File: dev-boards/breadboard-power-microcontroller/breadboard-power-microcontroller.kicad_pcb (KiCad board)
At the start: 2 copper layers, 51.3 x 22 mm, 28 parts, among them J0 USB_C_Receptacle_PowerOnly_6P, J1 Barrel_Jack_Switch, J2 Conn_01x02, Q1 AO3401A, Q2 AO3401A, SW1 SW_DPDT_x2, U1 AMS1117-5.0, U2 AMS1117-3.3

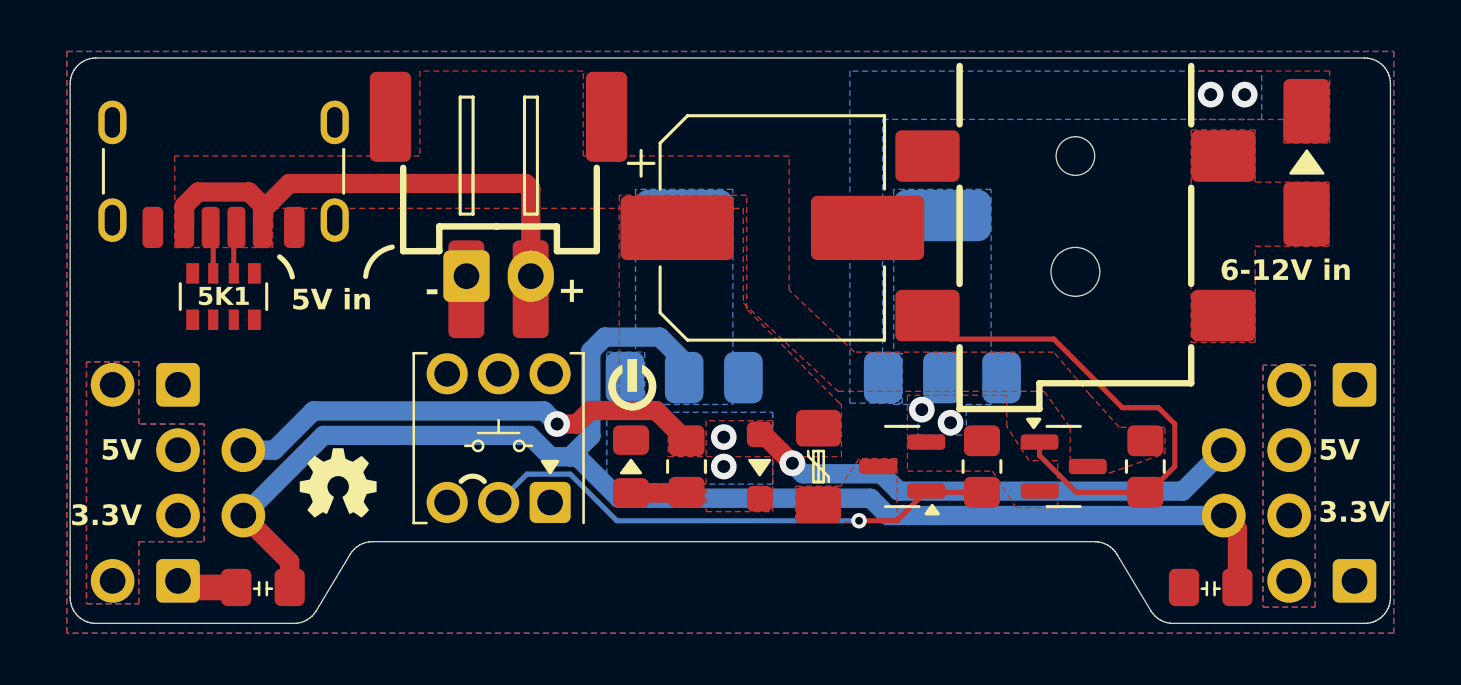
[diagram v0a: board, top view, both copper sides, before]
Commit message: Replace AMS1117 with MT6211 on breadboard microcontroller power board
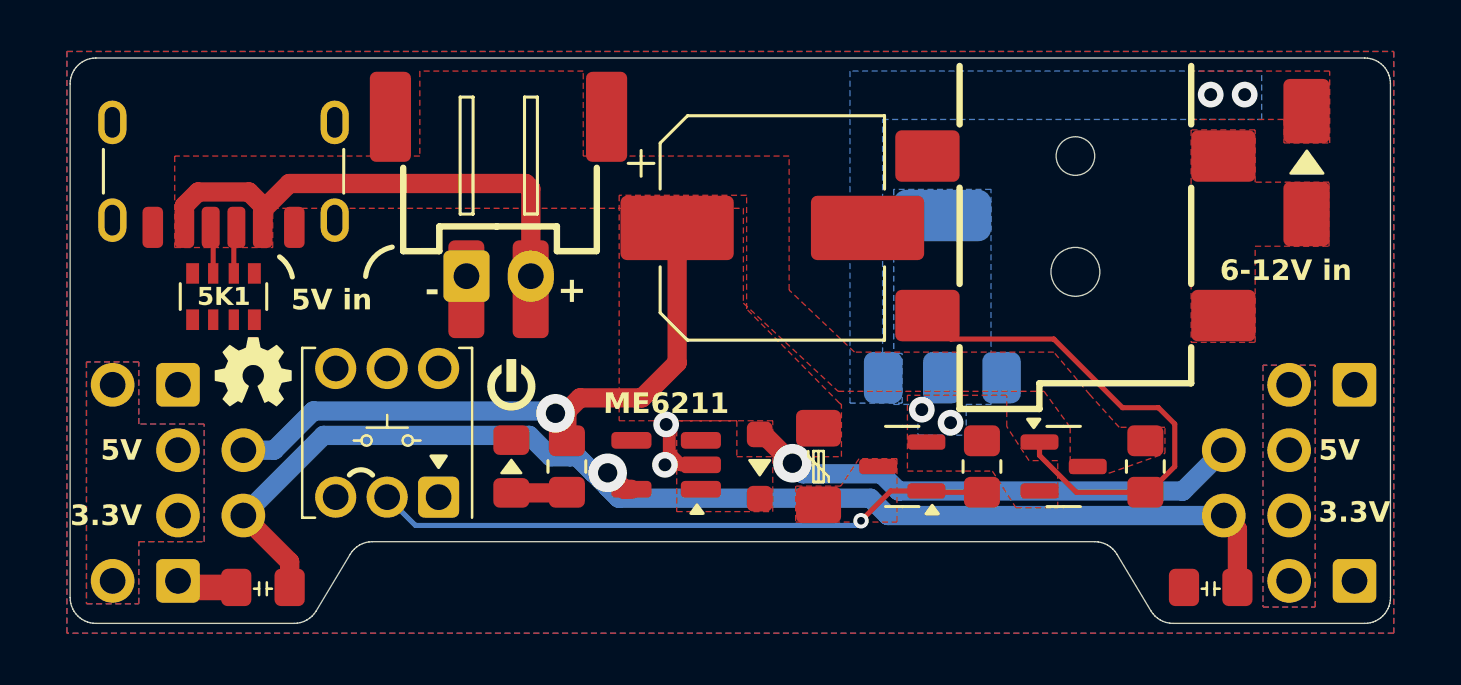
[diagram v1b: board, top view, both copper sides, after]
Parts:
- U2: value AMS1117-3.3 -> ME6211C33M5; footprint Package_TO_SOT_SMD:SOT-223-3_TabPin2 -> custom:SOT-23-5_HandSoldering_simple; moved to F.Cu
- moved U2 6.58 mm to (201.8, 92.0), turned to 180 degrees
- moved G*** 5.44 mm to (185.8, 88.4)
- moved G*** 4.70 mm to (195.8, 88.9)
- moved D3 4.65 mm to (195.8, 92.1)
- moved R6 4.65 mm to (198.0, 92.1)
- moved SW1 4.34 mm to (191.0, 90.8)
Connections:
- U2 pad 1: GND -> TO_3V3_DIODE
- U2 pad 2: 3V3_OUT -> GND
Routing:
- net 5V_OUT: track 38.4 -> 44.3 mm
- net 3V3_OUT: track 56.5 -> 51.0 mm, vias 0 -> 1
- net Net-(Q1-G): track 20.5 -> 24.1 mm
- net GND: track 2.55 -> 5.13 mm, vias 0 -> 2
- net TO_3V3_DIODE: track 0.22 -> 0.00 mm, vias 2 -> 0
- removed copper zone on B.Cu, net 3V3_OUT
- removed copper zone on B.Cu, net TO_3V3_DIODE
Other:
- board text added: "ME6211"
- board text removed: "AMS1117-3.3V"

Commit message: Rework traces and layout
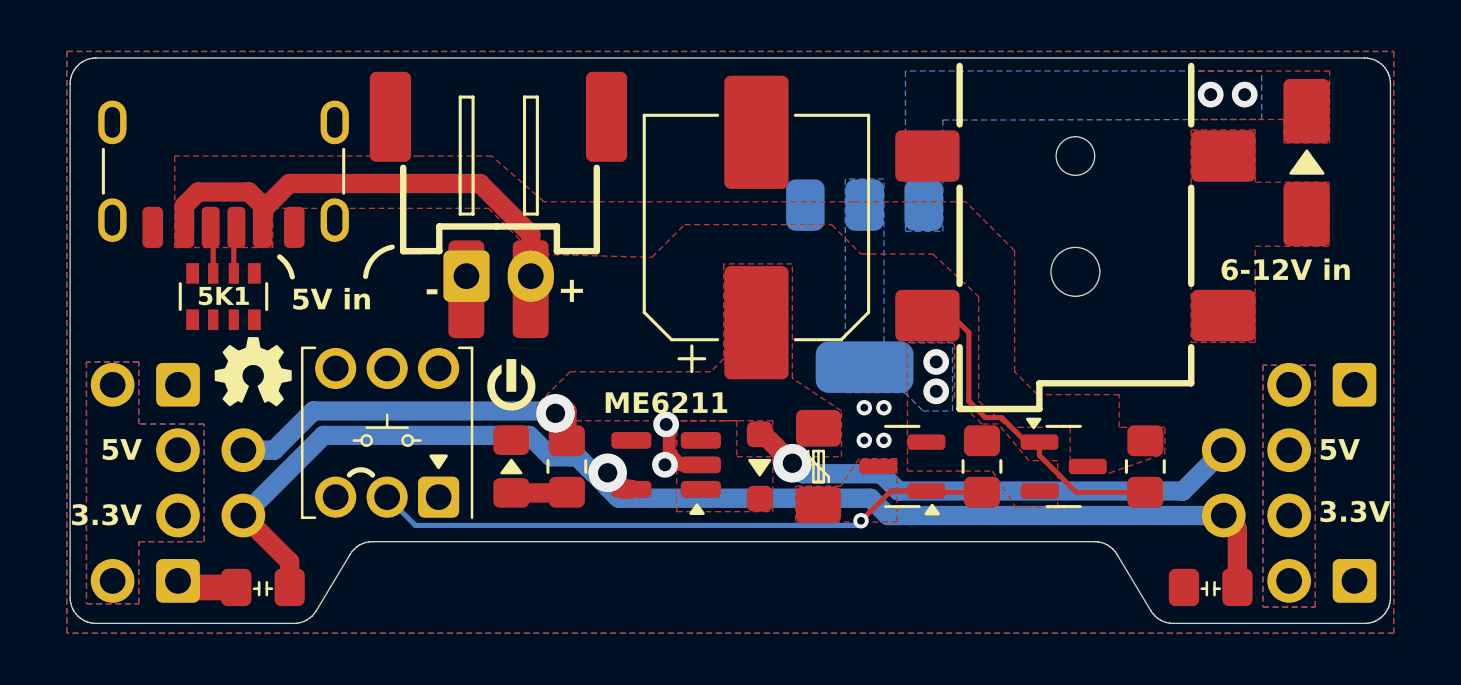
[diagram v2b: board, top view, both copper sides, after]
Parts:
- moved U1 3.05 mm to (209.6, 85.1), turned to -90 degrees
- moved C1 0.62 mm to (205.4, 82.8), turned to 90 degrees
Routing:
- net 5V_OUT: track 44.3 -> 34.0 mm
- net DC_JACK_SWITCH: track 19.8 -> 13.2 mm
- net VIN: track 20.2 -> 19.1 mm
- net GND: vias 2 -> 6
